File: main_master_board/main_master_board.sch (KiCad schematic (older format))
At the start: 6 parts, among them P5 Mounting Holes, P6 Mounting Holes, P7 Mounting Holes, P8 Mounting Holes

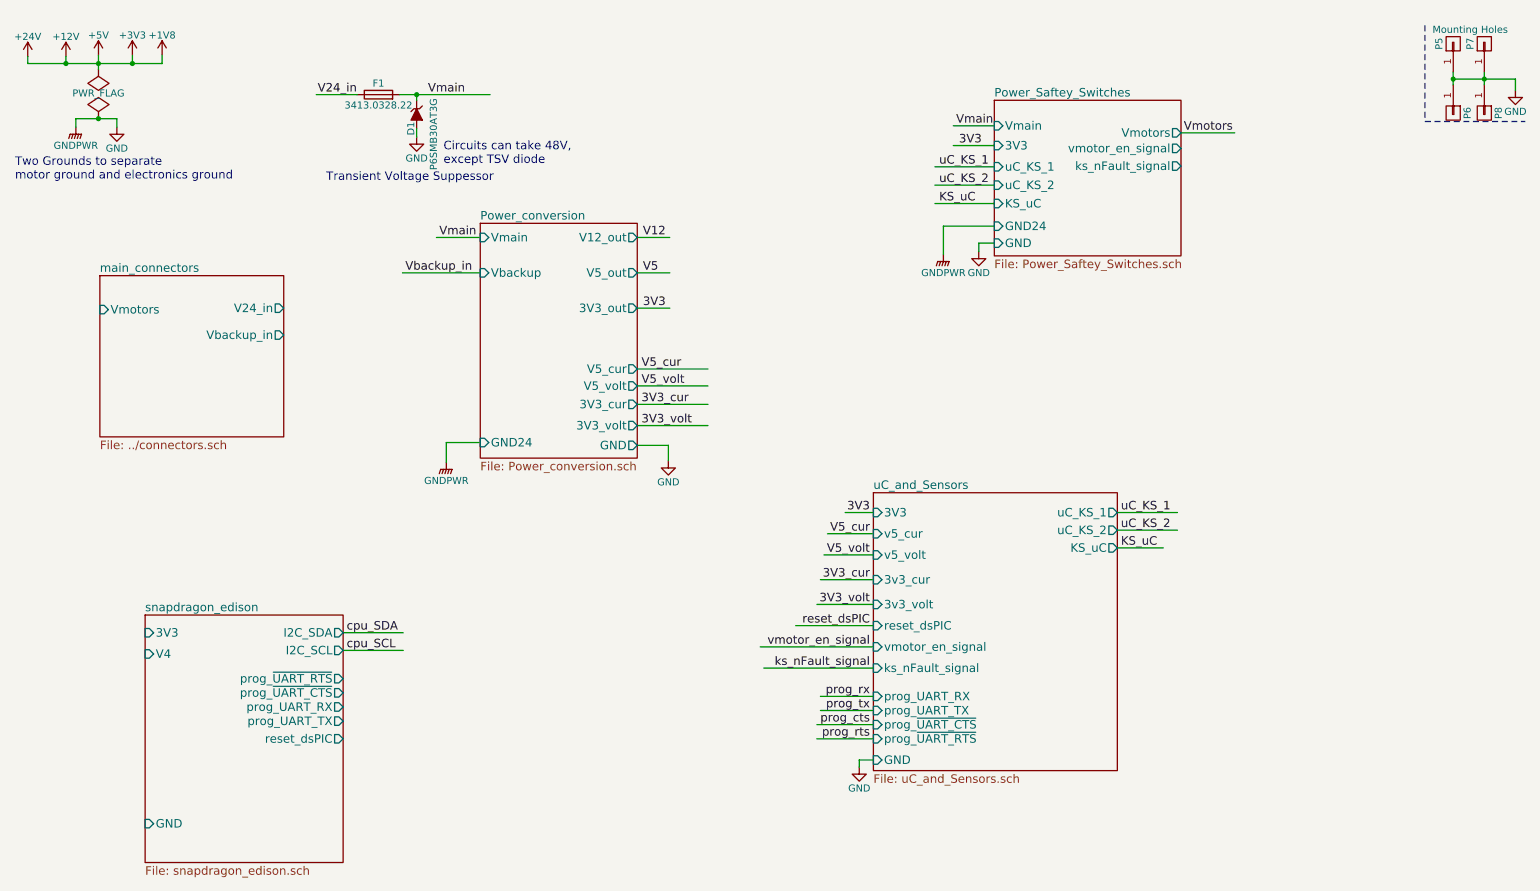
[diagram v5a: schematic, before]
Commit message: Working on moving things to two boards
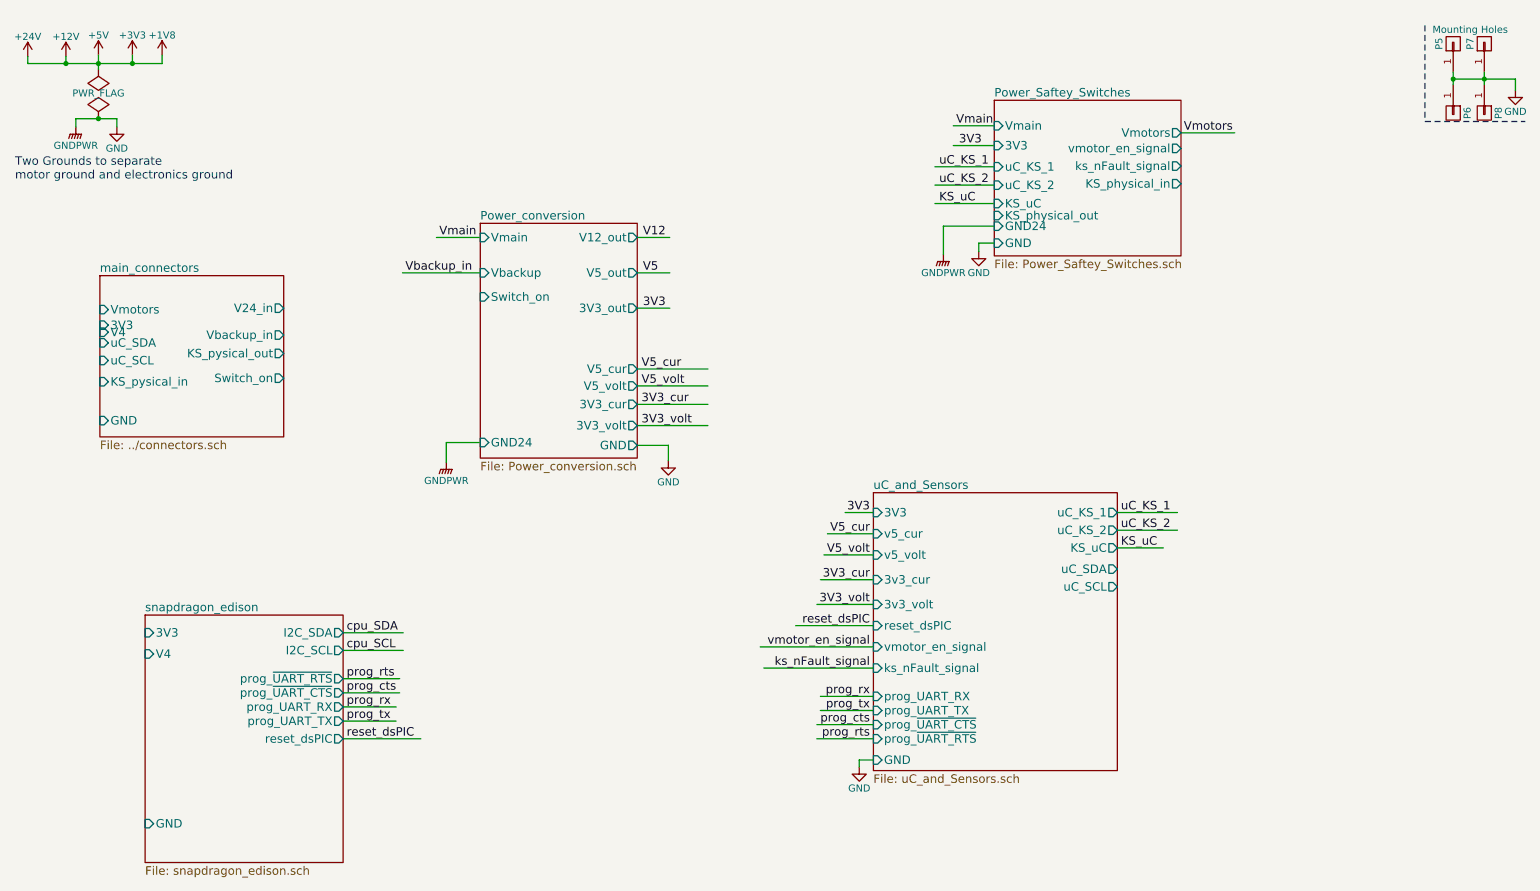
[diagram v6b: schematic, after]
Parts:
- removed D1: P6SMB30AT3G, Diodes_SMD:SMB_Standard, symbol ZENERsmall
- removed F1: 3413.0328.22, dp_devices:dp_devices-C1206, symbol Fuse
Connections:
- net labels removed: V24_in
- wire segments 59 -> 60
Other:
- note removed: "Circuits can take 48V, \nexcept TSV diode"
- note removed: "Transient Voltage Suppessor"
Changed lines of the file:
@@
 LIBS:FDS4935A
 LIBS:Si1900DL
-LIBS:Amplifiers
-LIBS:Connectors
-LIBS:DataStorage
-LIBS:Diodes
-LIBS:Microprocessors
-LIBS:MiscellaneousDevices
-LIBS:Passives
-LIBS:PMOD
-LIBS:PowerComponents
-LIBS:RepeaterParts
-LIBS:RF_OEM_Parts
 LIBS:Sensors
-LIBS:TransistorParts
 LIBS:LP3852-3.3
 LIBS:0s102011ma1qn1
@@
 LIBS:xal5050-562meb
 LIBS:xal6030-182mec
-LIBS:decaWave
 LIBS:conn_2x50
 LIBS:conn_open_q_x2
@@
 LIBS:ac-dc
 LIBS:actel
-LIBS:allegro
 LIBS:Altera
 LIBS:analog_devices
@@
 LIBS:logo
 LIBS:maxim
-LIBS:mechanical
 LIBS:microchip_dspic33dsc
 LIBS:microchip_pic10mcu
@@
 LIBS:microchip_pic32mcu
 LIBS:motor_drivers
-LIBS:motors
 LIBS:msp430
 LIBS:nordicsemi
@@
 LIBS:ttl_ieee
 LIBS:video
-LIBS:wiznet
 LIBS:Worldsemi
 LIBS:Xicor
-LIBS:zetex
 LIBS:Zilog
 LIBS:conn_2x45
@@
 F11 "3V3_volt" O R 4930 3310 60
 F12 "GND" O R 4930 3450 60
+F13 "Switch_on" I L 3820 2400 60
 $EndSheet
 Text Label 3290 2230 0    60   ~ 0
@@
 F10 "vmotor_en_signal" O R 8775 1350 60
 F11 "ks_nFault_signal" O R 8775 1475 60
+F12 "KS_physical_in" O R 8775 1600 60
+F13 "KS_physical_out" I L 7455 1825 60
 $EndSheet
 Text Label 3530 1980 0    60   ~ 0
 Vmain
-$Comp
-L ZENERsmall D1
-U 1 1 58700903
-P 3370 1110
-F 0 "D1" H 3470 1070 50  0000 C CNN
-F 1 "P6SMB30AT3G" H 3510 1230 50  0000 C CNN
-F 2 "Diodes_SMD:SMB_Standard" H 3370 1110 50  0001 C CNN
-F 3 "http://datasheet.octopart.com/P6SMB36AT3G-ON-Semiconductor-datasheet-5314825.pdf" H 3370 1110 50  0001 C CNN
-	1    3370 1110
-	0    1    1    0
-$EndComp
-$Comp
-L GND #PWR07
-U 1 1 5870090E
-P 3370 1270
-F 0 "#PWR07" H 3370 1020 50  0001 C CNN
-F 1 "GND" H 3370 1120 50  0000 C CNN
-F 2 "" H 3370 1270 50  0000 C CNN
-F 3 "" H 3370 1270 50  0000 C CNN
-	1    3370 1270
-	1    0    0    -1
-$EndComp
-Text Notes 2730 1590 0    60   ~ 0
-Transient Voltage Suppessor
-Text Label 3450 970  0    60   ~ 0
-Vmain
-Text Notes 3560 1470 0    60   ~ 0
-Circuits can take 48V, \nexcept TSV diode
-Text Label 2670 970  0    60   ~ 0
-V24_in
 Text Label 7185 1190 0    60   ~ 0
 Vmain
@@
 F16 "prog_~UART_CTS" I L 6600 5425 60
 F17 "prog_~UART_RTS" I L 6600 5525 60
+F18 "uC_SDA" O R 8325 4325 60
+F19 "uC_SCL" O R 8325 4450 60
 $EndSheet
 $Sheet
@@
 F3 "Vbackup_in" O R 2430 2670 60
 F4 "Vmotors" I L 1130 2490 60
+F5 "3V3" I L 1130 2600 60
+F6 "GND" I L 1130 3275 60
+F7 "uC_SDA" I L 1130 2725 60
+F8 "uC_SCL" I L 1130 2850 60
+F9 "KS_pysical_in" I L 1130 3000 60
+F10 "KS_pysical_out" O R 2430 2800 60
+F11 "V4" I L 1130 2650 60
+F12 "Switch_on" O R 2430 2975 60
 $EndSheet
 $Sheet
@@
 F11 "prog_~UART_RTS" O R 2850 5100 60
 $EndSheet
-$Comp
-L Fuse F1
-U 1 1 587AE04C
-P 3100 970
-F 0 "F1" V 3180 970 50  0000 C CNN
-F 1 "3413.0328.22" V 3025 970 50  0000 C CNN
-F 2 "dp_devices:dp_devices-C1206" V 3030 970 50  0001 C CNN
-F 3 "http://datasheet.octopart.com/3413.0328.22-Schurter-datasheet-8645987.pdf" H 3100 970 50  0001 C CNN
-	1    3100 970
-	0    -1   -1   0
-$EndComp
 Wire Wire Line
 	1120 690  1120 790
@@
 Wire Wire Line
 	3820 1980 3510 1980
-Wire Wire Line
-	3250 970  3890 970
-Wire Wire Line
-	3370 970  3370 1010
-Connection ~ 3370 970
-Wire Wire Line
-	3370 1210 3370 1270
-Wire Wire Line
-	2950 970  2660 970
 Wire Wire Line
 	7165 1190 7455 1190
@@
 Wire Wire Line
 	6600 4575 6200 4575
+Text Label 2875 5400 0    60   ~ 0
+prog_tx
+Text Label 2875 5300 0    60   ~ 0
+prog_rx
+Text Label 2875 5200 0    60   ~ 0
+prog_cts
+Text Label 2875 5100 0    60   ~ 0
+prog_rts
+Wire Wire Line
+	2850 5100 3250 5100
+Wire Wire Line
+	2850 5200 3250 5200
+Wire Wire Line
+	2850 5400 3225 5400
+Wire Wire Line
+	2850 5300 3225 5300
+Text Label 2875 5525 0    60   ~ 0
+reset_dsPIC
+Wire Wire Line
+	2850 5525 3400 5525
 $EndSCHEMATC

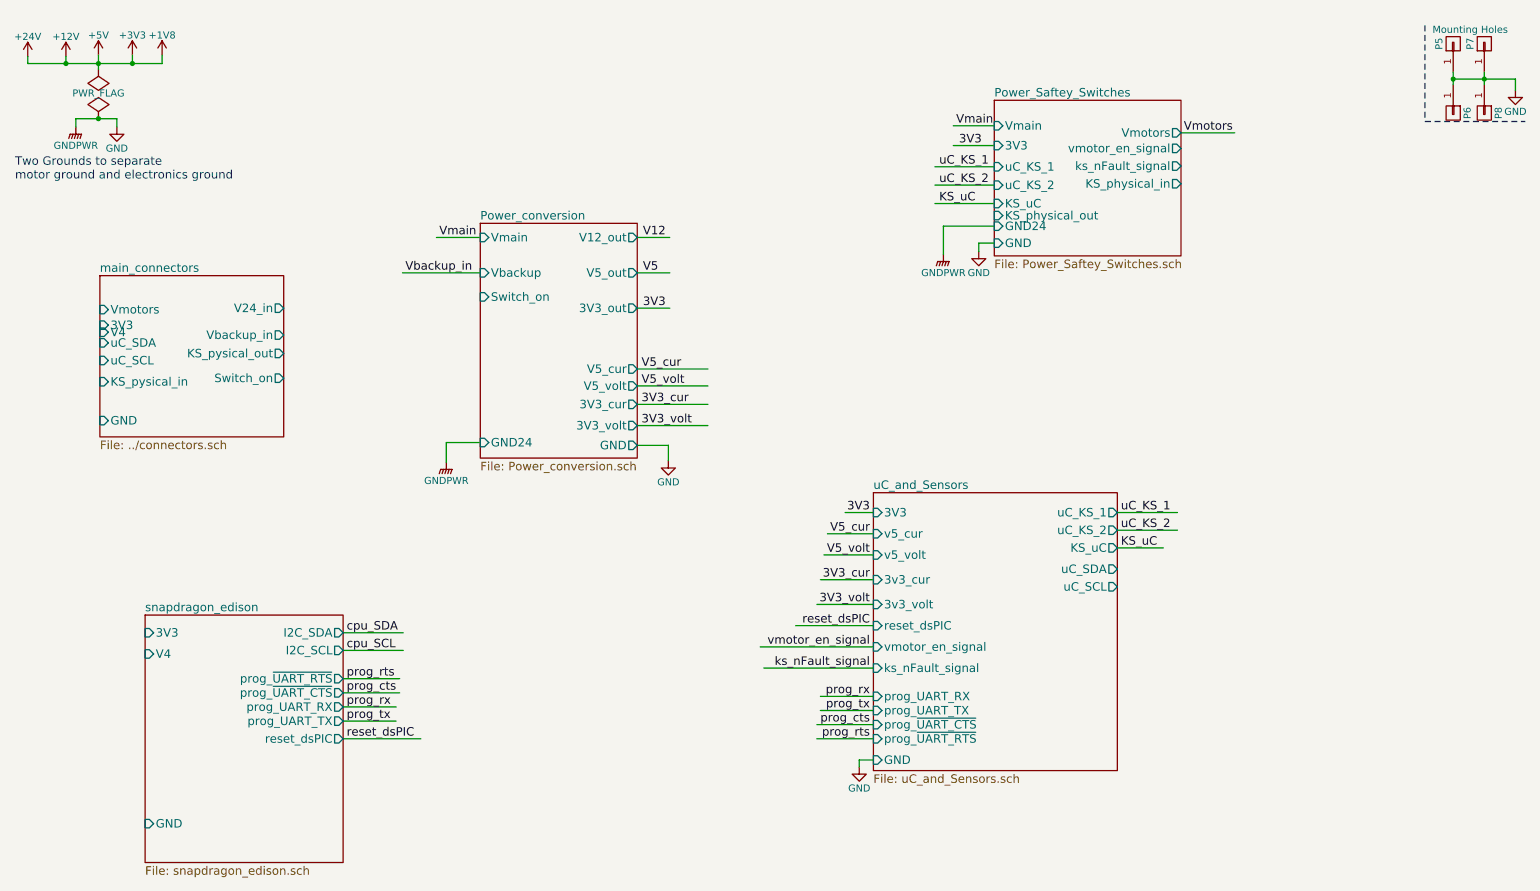
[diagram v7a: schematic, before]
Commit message: Added a lot of things. Put a 5v to 4v buck as well as supporing the snapdragon board
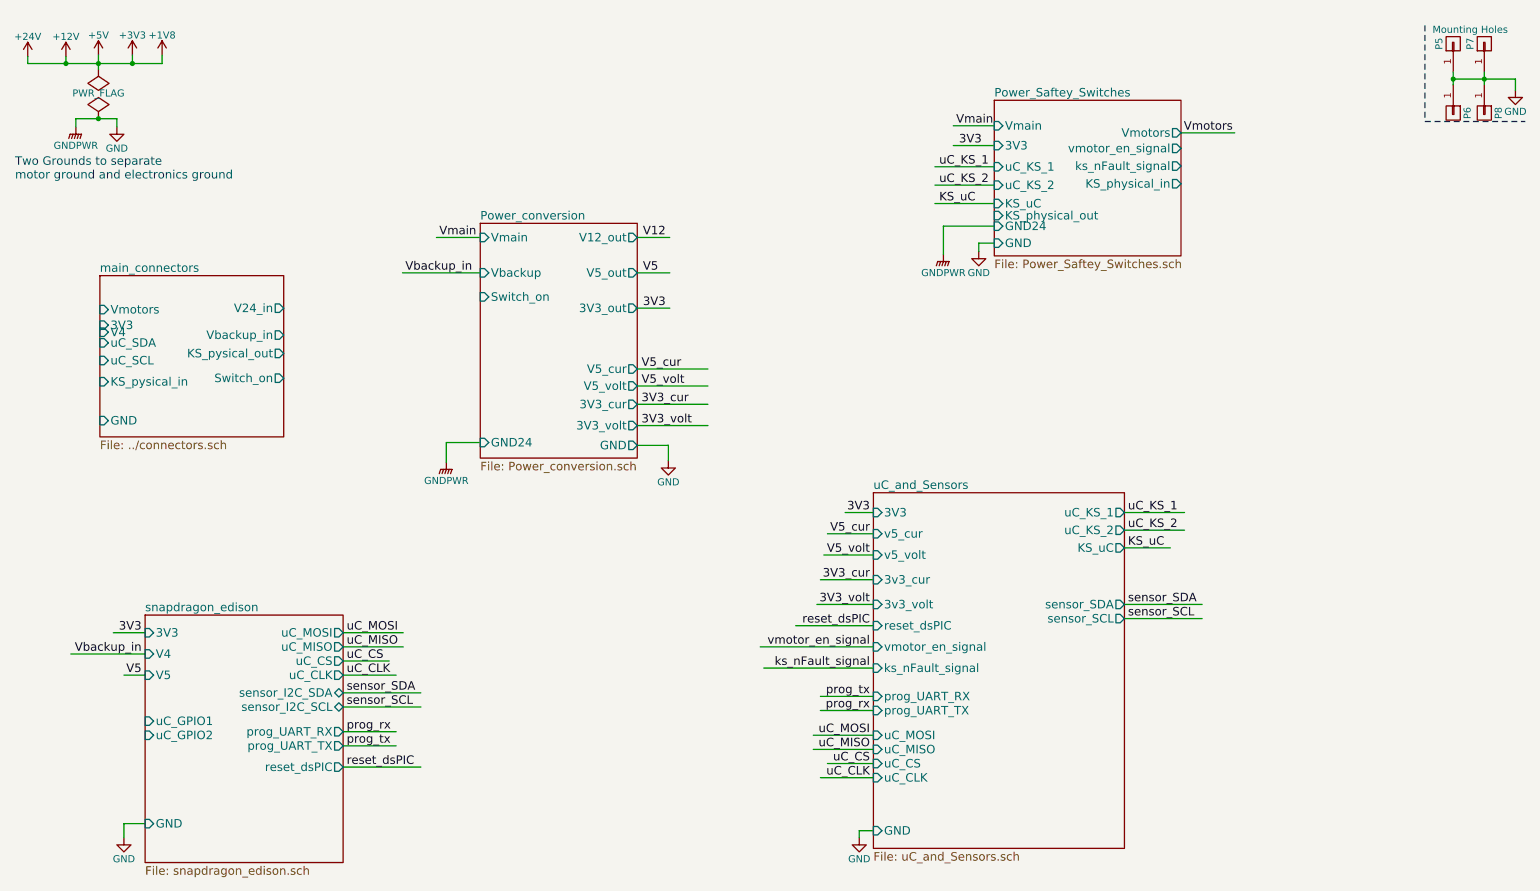
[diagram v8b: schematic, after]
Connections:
- net labels added: sensor_SCL, sensor_SDA, uC_CLK, uC_CS, uC_MISO, uC_MOSI
- net labels removed: cpu_SCL, cpu_SDA, prog_cts, prog_rts
- wire segments 60 -> 79
